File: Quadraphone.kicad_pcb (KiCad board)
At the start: 4 copper layers, 60 x 100 mm, 177 parts, among them J1 Conn_01x10_Male, J2 Conn_01x10_Male, J3 Conn_01x10_Male, J4 Conn_01x10_Male, J5 Eurorack_10_pin_power, U1 AMS1117-5.0, U10 TL072, U11 4066, U12 SSI2131, U13 TL072, U14 LM4040DBZ-2.5, U15 4066, U16 TL072, U17 SSI2131, U18 TL072, U22 SSI2131, U3 MCP6002, U4 LM4040DBZ-5, U5 MCP6004, U6 4066, U7 4066, U8 4066, U9 SSI2131

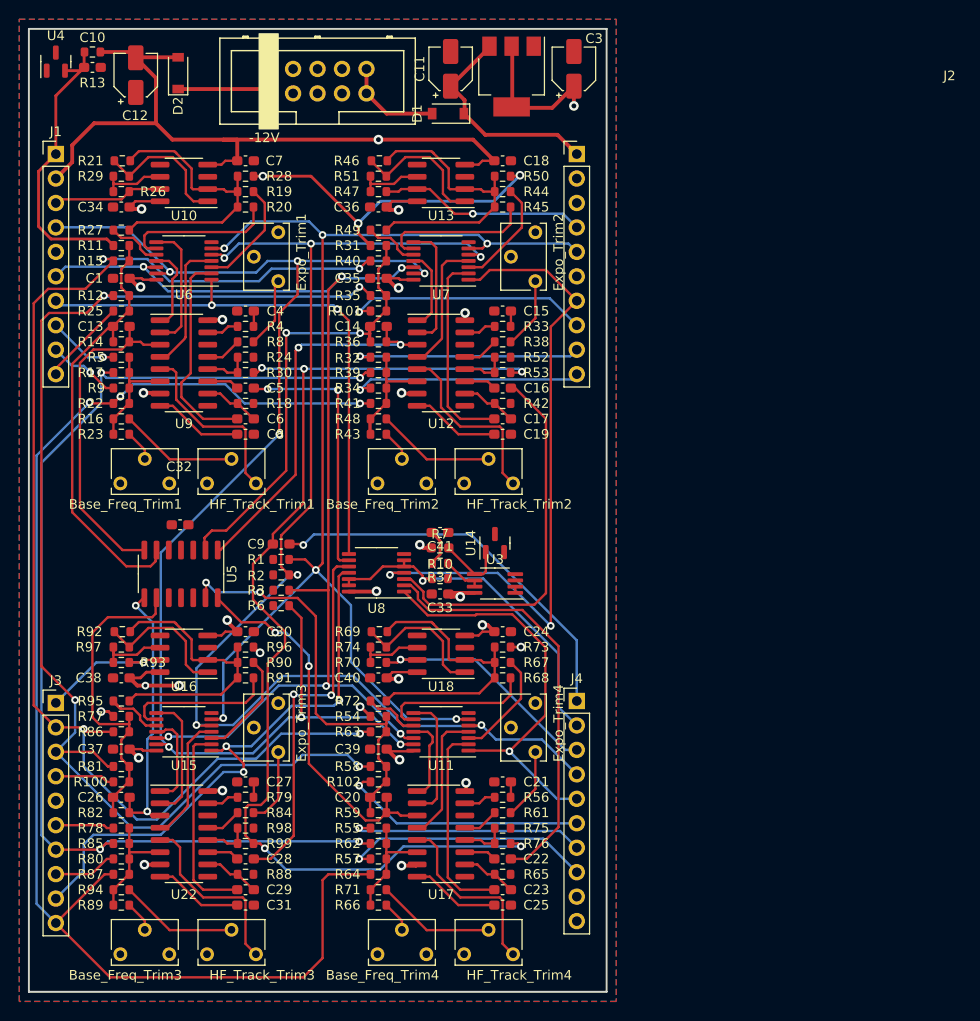
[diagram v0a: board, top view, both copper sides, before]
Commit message: Started control board schematic
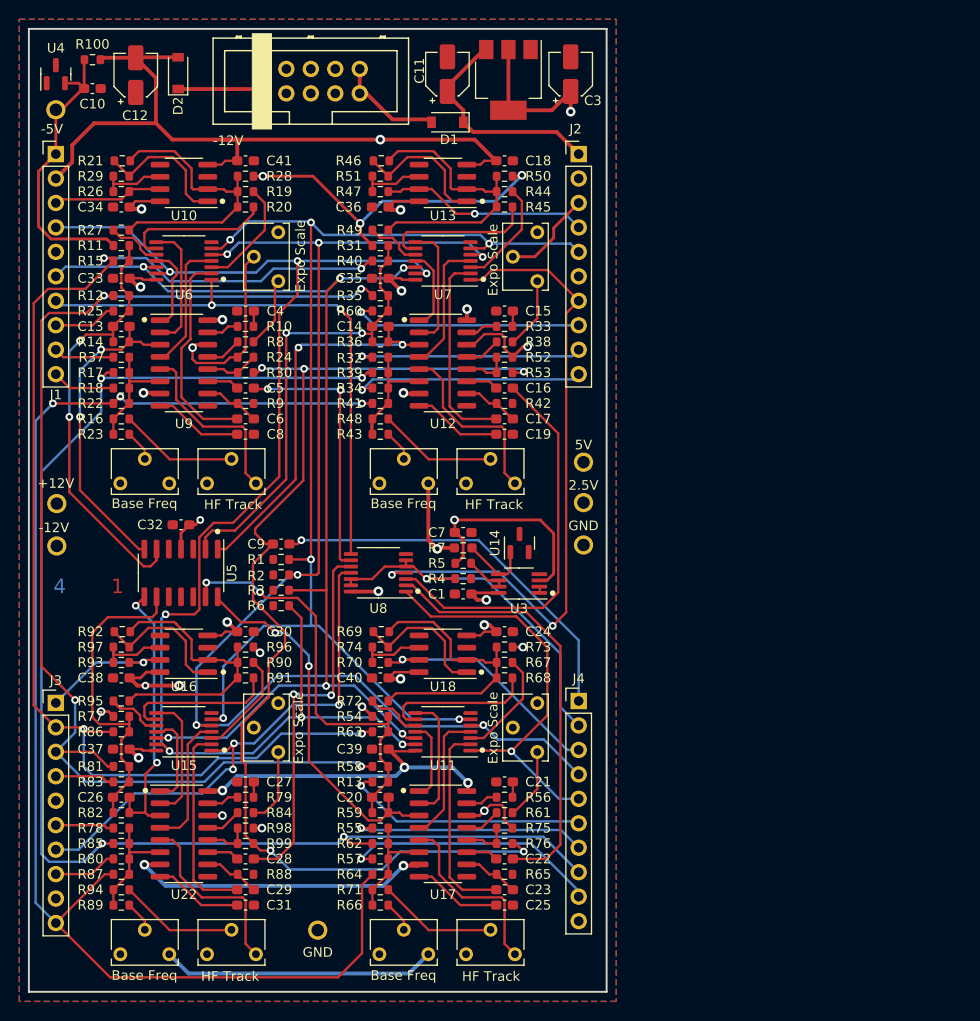
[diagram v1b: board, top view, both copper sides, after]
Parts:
- added FID1: 4_Layer_Marker, Custom_Footprints:4_Layer_Markers, F.Cu at (56.2, 107.9)
- added TP1: TestPoint, Custom_Footprints:1.3mm_Test_Point, F.Cu at (52.9, 99.3)
- added TP2: TestPoint, Custom_Footprints:1.3mm_Test_Point, F.Cu at (107.6, 95.0)
- added TP3: TestPoint, Custom_Footprints:1.3mm_Test_Point, F.Cu at (107.6, 99.2)
- added TP4: TestPoint, Custom_Footprints:1.3mm_Test_Point, F.Cu at (80.0, 143.6)
- added TP5: TestPoint, Custom_Footprints:1.3mm_Test_Point, F.Cu at (107.6, 103.6)
- added TP6: TestPoint, Custom_Footprints:1.3mm_Test_Point, F.Cu at (52.8, 58.4)
- added TP7: TestPoint, Custom_Footprints:1.3mm_Test_Point, F.Cu at (52.9, 103.7)
- R17, R39, R62, R85: value 49.9k -> 100k
- moved U14 2.55 mm to (101.0, 103.4)
- moved U3 2.50 mm to (100.9, 107.6)
- moved C1 2.40 mm to (95.1, 108.7)
- moved R4 2.40 mm to (95.1, 107.1)
- moved R5 2.40 mm to (95.1, 105.5)
- moved C7 2.40 mm to (95.1, 102.3)
- moved R7 2.40 mm to (95.1, 103.9)
- moved C10 2.20 mm to (56.6, 56.2)
- moved U4 1.30 mm to (52.8, 54.7)
- moved D1 0.90 mm to (93.5, 59.7)
- moved R100 0.80 mm to (56.6, 53.2)
- moved J5 0.70 mm to (74.2, 56.7)
- moved C11 0.64 mm to (93.5, 54.7)
- moved C3 0.64 mm to (106.3, 54.7)
- moved U1 0.48 mm to (99.8, 55.3)
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- renumbered C33 to C1, C1 to C33, C7 to C41, C41 to C7, R4 to R10, R13 to R100, R102 to R13, R9 to R18, R5 to R37, R10 to R4, R37 to R5, R101 to R60, R100 to R83, R18 to R9
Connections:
- J1 pad 10: /PWM_CV1 -> /FREQ_MOD1
- J1 pad 8: /V_PER_OCT1 -> /PWM_CV1
- J1 pad 9: /FREQ_MOD1 -> /V_PER_OCT1
- J3 pad 7: /FINE_TUNE -> /SYNCH_SIGNAL3
- J3 pad 9: /SYNCH_SIGNAL3 -> GND
- J4 pad 10: unconnected-(J4-Pad10) -> GND
- J4 pad 8: /FREQ_MOD4 -> /FINE_TUNE
- J4 pad 9: unconnected-(J4-Pad9) -> /FREQ_MOD4
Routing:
- net +2V5: track 3.90 -> 304.9 mm, vias 0 -> 7
- net /FINE_TUNE: track 117.2 -> 145.1 mm
- net +5V: track 300.4 -> 316.4 mm
- net -12V: track 266.7 -> 277.3 mm
- net /SYNCH_SIGNAL3: track 59.5 -> 54.6 mm
- net +12V: track 206.1 -> 211.0 mm
- net /PWM_POT: track 130.4 -> 125.7 mm
- net /PWM_CV: track 131.7 -> 128.2 mm
- net /HARD_SYNCH_SW: track 142.6 -> 145.9 mm
- net -5V: track 224.5 -> 227.0 mm
- net /PWM_CV1: track 9.03 -> 6.60 mm
- net /PULSE_SW: track 127.2 -> 125.0 mm
- net /Linear_Frequency: track 116.2 -> 118.1 mm
- net /OSCVoice1/PWM_Control: track 34.4 -> 32.9 mm, vias 0 -> 2
- net /SOFT_SYNCH_SW: track 37.2 -> 38.6 mm
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- added copper zone on In2.Cu, net GND
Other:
- board text added: "+12V"
- board text added: "-12V"
- board text added: "-5V"
- board text added: "2.5V"
- board text added: "5V"
- board text added: "Base Freq"
- board text added: "Expo Scale"
- board text added: "GND"
- board text added: "HF Track"

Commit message: Started laying out Panel
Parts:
- J1, J2, J3, J4: moved to B.Cu
- moved C11 0.07 mm to (93.4, 54.7)
- turned J1 to 180 degrees
- turned J2 to 180 degrees
- turned J3 to 180 degrees
- turned J4 to 180 degrees
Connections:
- J3 pad 10: /OCT_TUNE -> /FINE_TUNE
- J4 pad 8: /FINE_TUNE -> /OCT_TUNE
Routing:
- net /OCT_TUNE: track 141.2 -> 183.3 mm, vias 3 -> 4
- net /FINE_TUNE: track 145.1 -> 129.8 mm

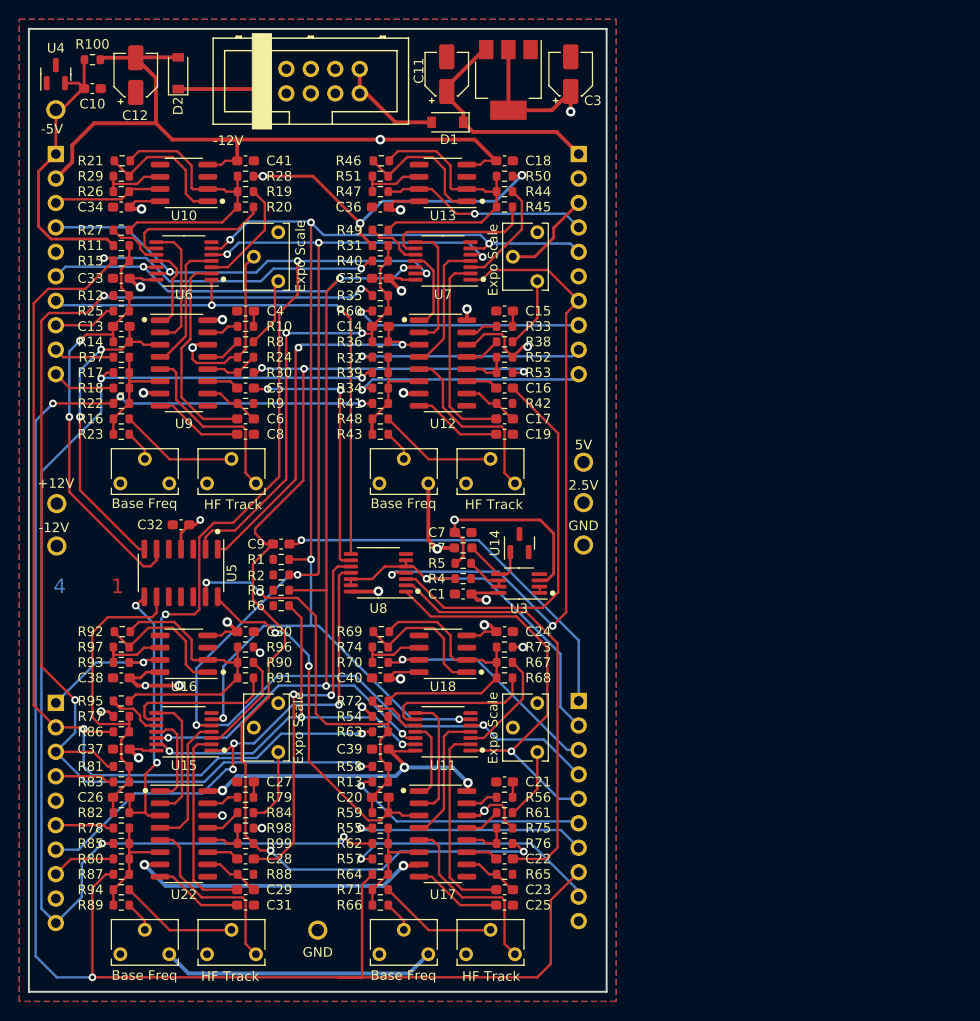
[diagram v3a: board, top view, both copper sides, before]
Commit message: Fixed ground connections on component board
Added JLC PCB plug-in
Schematic clean-up
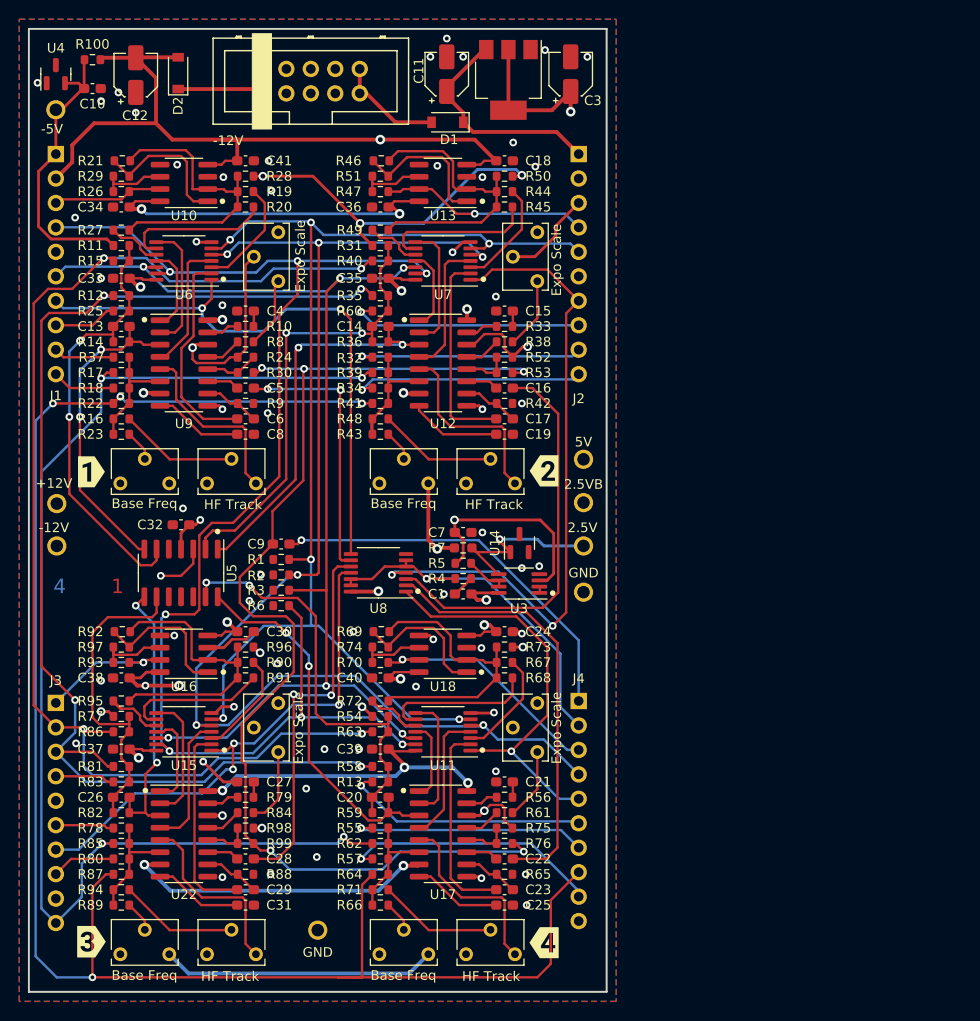
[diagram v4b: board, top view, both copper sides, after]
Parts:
- added TP8: TestPoint, Custom_Footprints:1.3mm_Test_Point, F.Cu at (107.6, 103.7)
- added kibuzzard-63D3EB0F: G***, kibuzzard-63D3EB0F, F.Cu at (103.5, 95.9)
- added kibuzzard-63D3EB2D: G***, kibuzzard-63D3EB2D, F.Cu at (56.5, 144.8)
- added kibuzzard-63D3EB3D: G***, kibuzzard-63D3EB3D, F.Cu at (103.5, 144.9)
- added kibuzzard-63D3EB53: G***, kibuzzard-63D3EB53, F.Cu at (56.5, 96.0)
- moved TP5 4.90 mm to (107.6, 108.5)
- moved TP2 0.30 mm to (107.6, 94.7)
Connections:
- net Net-(R7-Pad2) renamed /2.5V_Test
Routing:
- net GND: track 0.00 -> 34.3 mm, vias 0 -> 57
- net /2.5V_Test: track 7.11 -> 18.8 mm, vias 0 -> 1
- net +12V: track 211.1 -> 200.6 mm
- net /SYNCH_SIGNAL1: track 58.5 -> 61.6 mm
- net /Linear_Frequency: track 118.1 -> 120.1 mm
- net /OSCVoice2/Soft_Synch: track 40.9 -> 42.1 mm
- net +5V: track 316.4 -> 317.5 mm
- net /OSCVoice3/Pulse_Mix: track 16.0 -> 15.0 mm
- net /PWM_CV: track 128.2 -> 127.4 mm
- net /OSCVoice2/HF_Track: track 19.2 -> 19.9 mm
- net /OSCVoice1/MIX_1: track 14.6 -> 15.3 mm
- net /OSCVoice1/Op_Amp_Mix: track 30.2 -> 30.9 mm
- net /OSCVoice3/Op_Amp_Mix: track 30.0 -> 30.7 mm
- net /OSCVoice2/MIX_1: track 14.6 -> 15.2 mm
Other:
- board text added: "2.5VB"
- board text added: "Quadraphone Components v1.0 Mountjoy Modular"

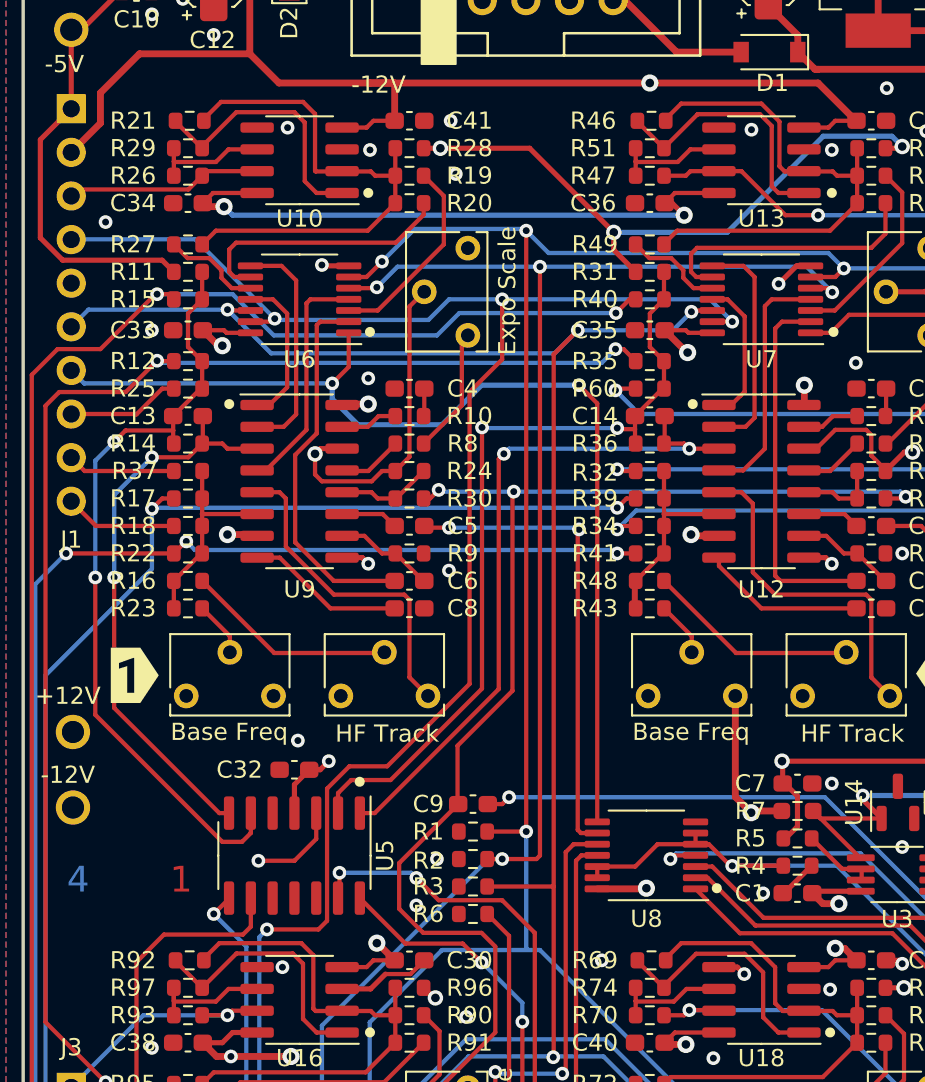
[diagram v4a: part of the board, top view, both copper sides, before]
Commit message: Added RJ45 breakout module
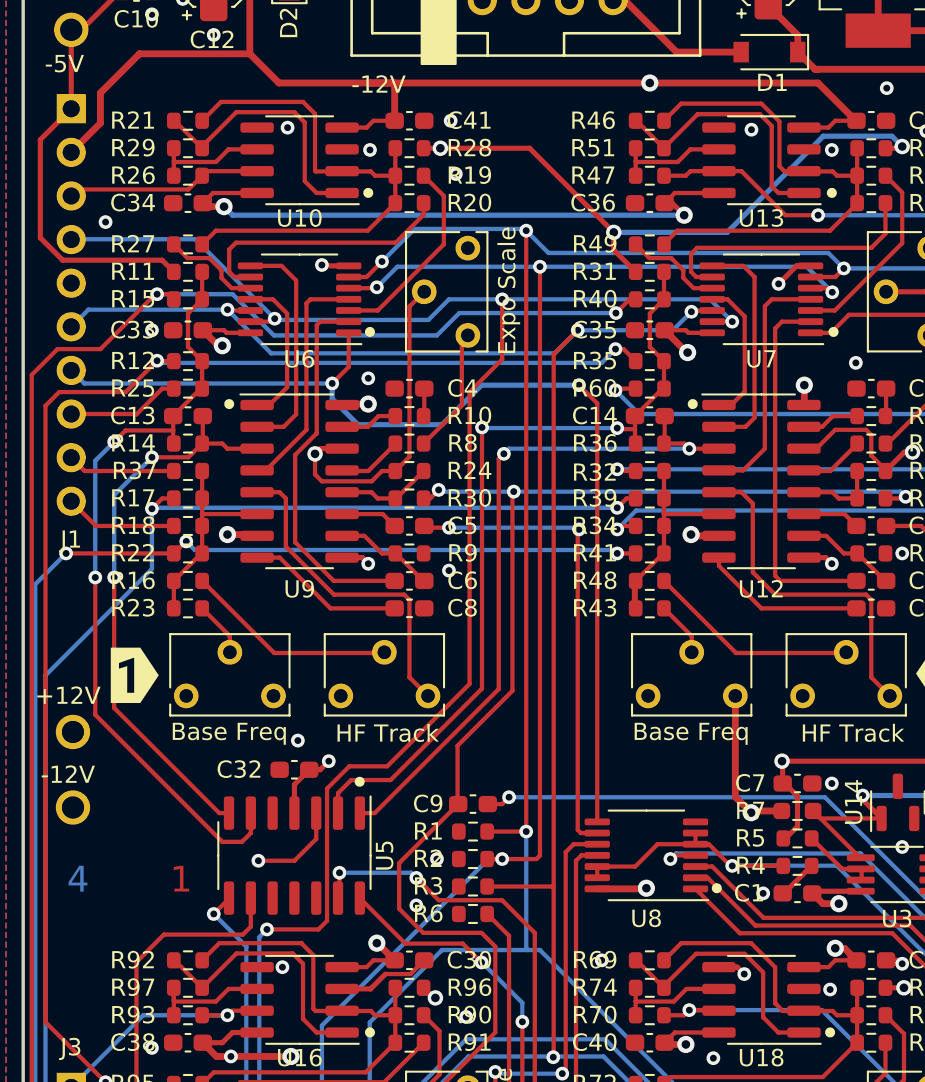
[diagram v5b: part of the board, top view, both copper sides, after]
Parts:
- moved R21 0.10 mm to (59.6, 63.7)
- moved R92 0.10 mm to (59.6, 112.6)
- moved R46 0.10 mm to (86.5, 63.7)
- moved R69 0.10 mm to (86.5, 112.6)
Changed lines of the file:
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@@
     (40 "Dwgs.User" user "User.Drawings")
     (41 "Cmts.User" user "User.Comments")
-    (42 "Eco1.User" user "User.Eco1")
-    (43 "Eco2.User" user "User.Eco2")
     (44 "Edge.Cuts" user)
     (45 "Margin" user)
@@
     (48 "B.Fab" user)
     (49 "F.Fab" user)
-    (50 "User.1" user)
-    (51 "User.2" user)
-    (52 "User.3" user)
-    (53 "User.4" user)
-    (54 "User.5" user)
-    (55 "User.6" user)
-    (56 "User.7" user)
-    (57 "User.8" user)
-    (58 "User.9" user)
   )
   (setup
@@
     (property "Sheetname" "")
     (attr smd)
-    (fp_text reference "R2" (at -2.6 0.1) (layer "F.SilkS")
+    (fp_text reference "R2" (at -2.6 0) (layer "F.SilkS")
       (effects (font (size 1 1) (thickness 0.15)))
     )
@@
   )
   (footprint "Resistor_SMD:R_0603_1608Metric" (layer "F.Cu")
-    (at 95.1 107.087291 180)
+    (at 95.1 107.1 180)
     (descr "Resistor SMD 0603 (1608 Metric), square (rectangular) end terminal, IPC_7351 nominal, (Body size source: IPC-SM-782 page 72, https://www.pcb-3d.com/wordpress/wp-content/uploads/ipc-sm-782a_amendment_1_and_2.pdf), generated with kicad-footprint-generator")
     (tags "resistor")
@@
     (property "Sheetname" "")
     (attr smd)
-    (fp_text reference "R4" (at 2.7375 -0.012709) (layer "F.SilkS")
+    (fp_text reference "R4" (at 2.7375 0) (layer "F.SilkS")
       (effects (font (size 1 1) (thickness 0.15)))
     )
@@
   )
   (footprint "Resistor_SMD:R_0603_1608Metric" (layer "F.Cu")
-    (at 59.7 63.7)
+    (at 59.6 63.7)
     (descr "Resistor SMD 0603 (1608 Metric), square (rectangular) end terminal, IPC_7351 nominal, (Body size source: IPC-SM-782 page 72, https://www.pcb-3d.com/wordpress/wp-content/uploads/ipc-sm-782a_amendment_1_and_2.pdf), generated with kicad-footprint-generator")
     (tags "resistor")
@@
     (property "Sheetname" "OSCVoice1")
     (attr smd)
-    (fp_text reference "R21" (at -3.3 0) (layer "F.SilkS")
+    (fp_text reference "R21" (at -3.2 0) (layer "F.SilkS")
       (effects (font (size 1 1) (thickness 0.15)))
     )
@@
   )
   (footprint "Resistor_SMD:R_0603_1608Metric" (layer "F.Cu")
-    (at 59.7 112.6)
+    (at 59.6 112.6)
     (descr "Resistor SMD 0603 (1608 Metric), square (rectangular) end terminal, IPC_7351 nominal, (Body size source: IPC-SM-782 page 72, https://www.pcb-3d.com/wordpress/wp-content/uploads/ipc-sm-782a_amendment_1_and_2.pdf), generated with kicad-footprint-generator")
     (tags "resistor")
@@
     (property "Sheetname" "OSCVoice3")
     (attr smd)
-    (fp_text reference "R92" (at -3.3 0) (layer "F.SilkS")
+    (fp_text reference "R92" (at -3.2 0) (layer "F.SilkS")
       (effects (font (size 1 1) (thickness 0.15)))
     )
@@
   )
   (footprint "Resistor_SMD:R_0603_1608Metric" (layer "F.Cu")
-    (at 95.102149 105.5 180)
+    (at 95.1 105.5 180)
     (descr "Resistor SMD 0603 (1608 Metric), square (rectangular) end terminal, IPC_7351 nominal, (Body size source: IPC-SM-782 page 72, https://www.pcb-3d.com/wordpress/wp-content/uploads/ipc-sm-782a_amendment_1_and_2.pdf), generated with kicad-footprint-generator")
     (tags "resistor")
@@
   )
   (footprint "Capacitor_SMD:C_0603_1608Metric_Pad1.08x0.95mm_HandSolder" (layer "F.Cu")
-    (at 95.1 108.687291 180)
+    (at 95.1 108.7 180)
     (descr "Capacitor SMD 0603 (1608 Metric), square (rectangular) end terminal, IPC_7351 nominal with elongated pad for handsoldering. (Body size source: IPC-SM-782 page 76, https://www.pcb-3d.com/wordpress/wp-content/uploads/ipc-sm-782a_amendment_1_and_2.pdf), generated with kicad-footprint-generator")
     (tags "capacitor handsolder")
@@
     (property "Sheetname" "")
     (attr smd)
-    (fp_text reference "C1" (at 2.7375 -0.012709) (layer "F.SilkS")
+    (fp_text reference "C1" (at 2.8 0) (layer "F.SilkS")
       (effects (font (size 1 1) (thickness 0.15)))
     )
@@
   )
   (footprint "Resistor_SMD:R_0603_1608Metric" (layer "F.Cu")
-    (at 86.6 112.6)
+    (at 86.5 112.6)
     (descr "Resistor SMD 0603 (1608 Metric), square (rectangular) end terminal, IPC_7351 nominal, (Body size source: IPC-SM-782 page 72, https://www.pcb-3d.com/wordpress/wp-content/uploads/ipc-sm-782a_amendment_1_and_2.pdf), generated with kicad-footprint-generator")
     (tags "resistor")
@@
     (property "Sheetname" "OSCVoice4")
     (attr smd)
-    (fp_text reference "R69" (at -3.3 0) (layer "F.SilkS")
+    (fp_text reference "R69" (at -3.2 0) (layer "F.SilkS")
       (effects (font (size 1 1) (thickness 0.15)))
     )
@@
   )
   (footprint "Resistor_SMD:R_0603_1608Metric" (layer "F.Cu")
-    (at 86.6 63.7)
+    (at 86.5 63.7)
     (descr "Resistor SMD 0603 (1608 Metric), square (rectangular) end terminal, IPC_7351 nominal, (Body size source: IPC-SM-782 page 72, https://www.pcb-3d.com/wordpress/wp-content/uploads/ipc-sm-782a_amendment_1_and_2.pdf), generated with kicad-footprint-generator")
     (tags "resistor")
@@
     (property "Sheetname" "OSCVoice2")
     (attr smd)
-    (fp_text reference "R46" (at -3.4 0) (layer "F.SilkS")
+    (fp_text reference "R46" (at -3.3 0) (layer "F.SilkS")
       (effects (font (size 1 1) (thickness 0.15)))
     )
